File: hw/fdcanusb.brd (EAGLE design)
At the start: 41 x 32 mm, 37 parts, among them J1 MF-CON-MICROUSB-RIGHT, J3 JST-ZH6SMT_VERT, M1 MOUNT, M2 MOUNT, M3 MOUNT, M4 MOUNT, U1 MF-REG-SOT235-3.3V-300mA, U2 USBLC6-2SC6, U3 TCAN334G, U4 TLP3317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

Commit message: Fix resistor footprint
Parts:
- R5: device mfpassives:R0805 -> mfpassives:R0603
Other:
- board text added: "mjbots fdcanusb r2.5 (c) 2021"
- board text removed: "mjbots fdcanusb r2.4 (c) 2021"
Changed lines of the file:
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@@
 <wire x1="41" y1="32" x2="0" y2="32" width="0" layer="20"/>
 <wire x1="0" y1="32" x2="0" y2="0" width="0" layer="20"/>
-<text x="10" y="24.4" size="1" layer="21">mjbots fdcanusb r2.4
+<text x="10" y="24.4" size="1" layer="21">mjbots fdcanusb r2.5
 (c) 2021</text>
 <text x="2.5" y="7.2" size="0.8" layer="21" rot="R180">G</text>
@@
 <attribute name="POPULATE" value="0" x="5" y="8" size="1.778" layer="27" display="off"/>
 </element>
-<element name="R5" library="mfpassives" package="R0805" value="120" x="28.5" y="22.4" smashed="yes" rot="R90">
+<element name="R5" library="mfpassives" package="R0603" value="120" x="28.5" y="22.4" smashed="yes" rot="R90">
 <attribute name="HOUSEPART" value="" x="28.5" y="22.4" size="1.778" layer="27" rot="R90" display="off"/>
 <attribute name="MF" value="YAGEO" x="28.5" y="22.4" size="1.778" layer="27" rot="R90" display="off"/>
@@
 <wire x1="23.7317" y1="25.3067" x2="23.285" y2="24.86" width="0.2159" layer="1"/>
 <wire x1="23.7317" y1="26.1525625" x2="23.7317" y2="25.3067" width="0.2159" layer="1"/>
-<wire x1="28.5" y1="21.45" x2="28.5" y2="20.5683" width="0.2159" layer="1"/>
+<wire x1="28.5" y1="21.65" x2="28.5" y2="20.5683" width="0.2159" layer="1"/>
 </signal>
 <signal name="N$3">
@@
 <contactref element="R5" pad="P$2"/>
 <contactref element="U4" pad="3"/>
-<wire x1="28.5" y1="23.35" x2="29.45" y2="23.35" width="0.254" layer="1"/>
-<wire x1="29.45" y1="23.35" x2="29.8" y2="23" width="0.254" layer="1"/>
+<wire x1="28.5" y1="23.15" x2="29.742678125" y2="23.15" width="0.254" layer="1"/>
+<wire x1="29.767390625" y1="23.032609375" x2="29.742678125" y2="23.15" width="0.254" layer="1"/>
+<wire x1="29.8" y1="23" x2="29.767390625" y2="23.032609375" width="0.254" layer="1"/>
 <via x="29.8" y="23" extent="1-16" drill="0.35"/>
 <wire x1="29.8" y1="23" x2="29.8" y2="19" width="0.254" layer="16"/>

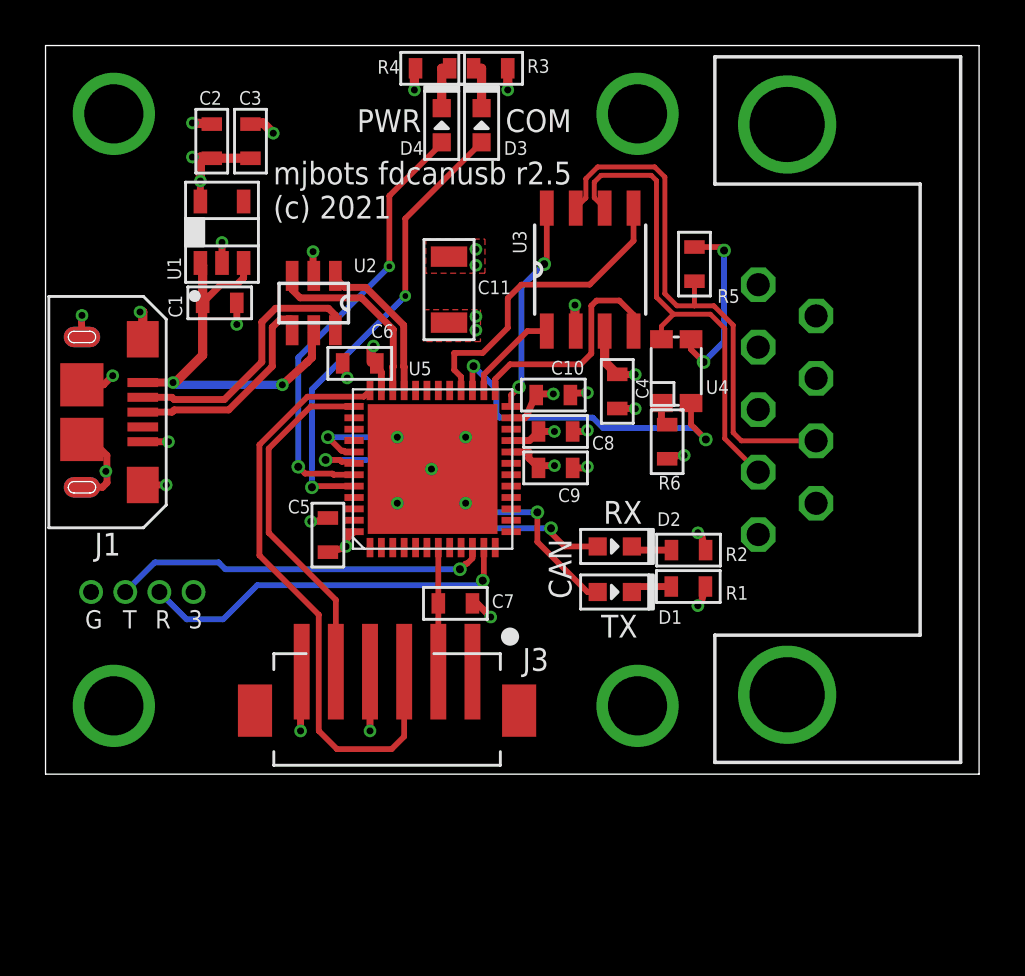
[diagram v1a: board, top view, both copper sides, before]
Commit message: SCHEMATIC ONLY work on more CAN transceiver variants
Update schematic, but not PCB, to accept the TCAN1057AEV in addition
to the 3.3V native variants.
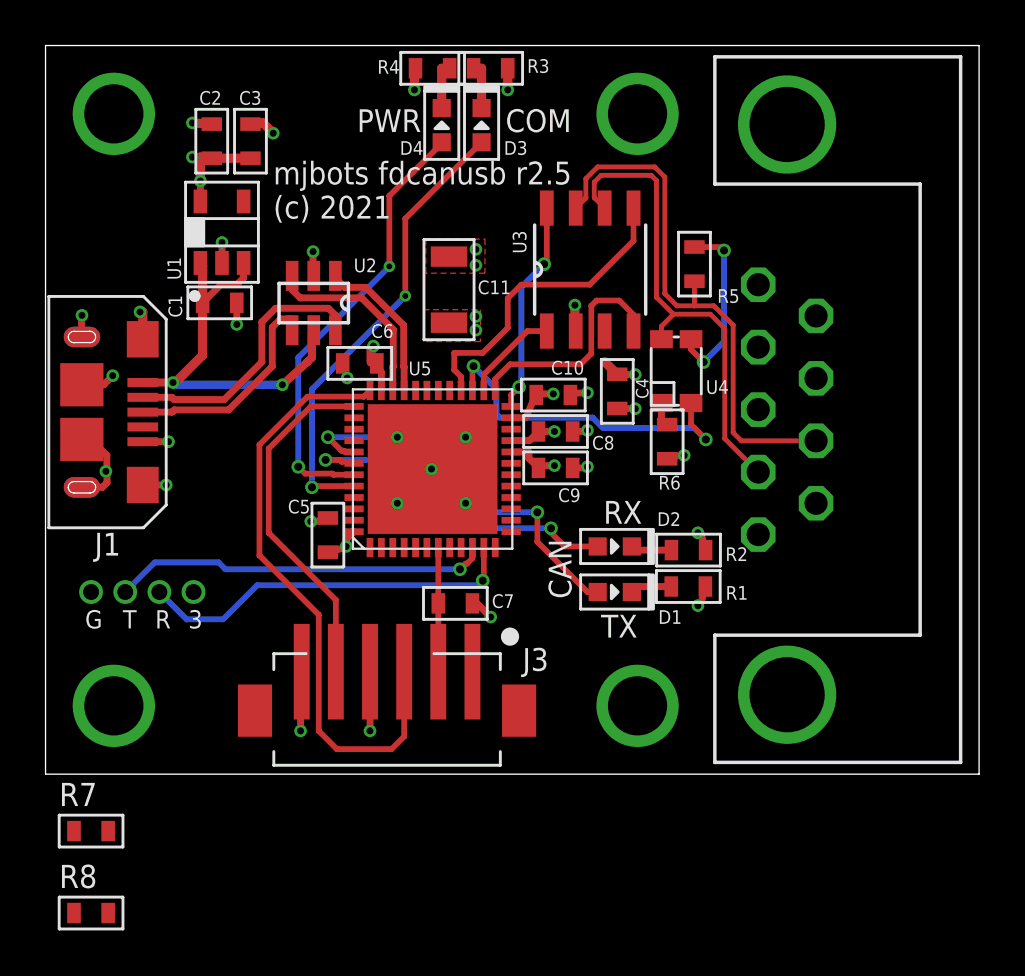
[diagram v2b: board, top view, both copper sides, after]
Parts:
- added R7: DNP, mfpassives:R0603
- added R8: 0, mfpassives:R0603
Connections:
- new net N$1: R7.P$2, R8.P$2, U3.3
- net +3V3: now also R7.P$1; no longer U3.3
- net VBUS: now also R8.P$1
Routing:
- net +3V3: track 22.2 -> 20.9 mm
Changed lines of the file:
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@@
 <param name="tpViaShape" value="round"/>
 <param name="PrefDir.1" value="|"/>
-<param name="PrefDir.2" value="/"/>
+<param name="PrefDir.2" value="0"/>
 <param name="PrefDir.3" value="0"/>
 <param name="PrefDir.4" value="0"/>
@@
 <param name="PrefDir.13" value="0"/>
 <param name="PrefDir.14" value="0"/>
-<param name="PrefDir.15" value="\"/>
+<param name="PrefDir.15" value="0"/>
 <param name="PrefDir.16" value="-"/>
 <param name="cfVia" value="8"/>
@@
 <attribute name="VOLTAGE" value="" x="27.3" y="14.6" size="1.778" layer="27" rot="R90" display="off"/>
 <attribute name="WATTAGE" value="" x="27.3" y="14.6" size="1.778" layer="27" rot="R90" display="off"/>
+</element>
+<element name="R7" library="mfpassives" package="R0603" value="DNP" x="2" y="-2.5" smashed="yes">
+<attribute name="HOUSEPART" value="YES" x="2" y="-2.5" size="1.778" layer="27" display="off"/>
+<attribute name="MPN" value="" x="2" y="-2.5" size="1.778" layer="27" display="off"/>
+<attribute name="NAME" x="0.6" y="-1.4" size="1.016" layer="25" font="vector" ratio="16"/>
+<attribute name="POPULATE" value="0" x="2" y="-2.5" size="1.778" layer="27" display="off"/>
+<attribute name="TOLERANCE" value="" x="2" y="-2.5" size="1.778" layer="27" display="off"/>
+<attribute name="URL" value="" x="2" y="-2.5" size="1.778" layer="27" display="off"/>
+<attribute name="VOLTAGE" value="" x="2" y="-2.5" size="1.778" layer="27" display="off"/>
+<attribute name="WATTAGE" value="" x="2" y="-2.5" size="1.778" layer="27" display="off"/>
+</element>
+<element name="R8" library="mfpassives" package="R0603" value="0" x="2" y="-6.1" smashed="yes">
+<attribute name="HOUSEPART" value="YES" x="2" y="-6.1" size="1.778" layer="27" display="off"/>
+<attribute name="MPN" value="MF-RES-0603-0" x="2" y="-6.1" size="1.778" layer="27" display="off"/>
+<attribute name="NAME" x="0.6" y="-5" size="1.016" layer="25" font="vector" ratio="16"/>
+<attribute name="POPULATE" value="1" x="2" y="-6.1" size="1.778" layer="27" display="off"/>
+<attribute name="TOLERANCE" value="" x="2" y="-6.1" size="1.778" layer="27" display="off"/>
+<attribute name="URL" value="" x="2" y="-6.1" size="1.778" layer="27" display="off"/>
+<attribute name="VOLTAGE" value="" x="2" y="-6.1" size="1.778" layer="27" display="off"/>
+<attribute name="WATTAGE" value="" x="2" y="-6.1" size="1.778" layer="27" display="off"/>
 </element>
 </elements>
@@
 <wire x1="10.4" y1="17.1" x2="5.7" y2="17.1" width="0.3556" layer="16"/>
 <wire x1="5.7" y1="17.1" x2="5.6" y2="17.2" width="0.3556" layer="16"/>
+<contactref element="R8" pad="P$1"/>
+<wire x1="1.25" y1="-6.1" x2="4.27" y2="17.2" width="0" layer="19" extent="1-1"/>
 </signal>
 <signal name="USB_D_N" class="1">
@@
 <contactref element="C3" pad="P$1"/>
 <contactref element="C4" pad="P$1"/>
-<contactref element="U3" pad="3"/>
 <contactref element="C8" pad="P$1"/>
 <contactref element="C9" pad="P$1"/>
@@
 <wire x1="13.2" y1="10" x2="13.2" y2="10.3" width="0.3048" layer="1"/>
 <wire x1="13.2" y1="10.3" x2="13.55" y2="10.65" width="0.3048" layer="1"/>
-<wire x1="24.555" y1="19.46" x2="24.555" y2="18.115" width="0.4064" layer="1"/>
 <wire x1="24.555" y1="18.115" x2="25.11" y2="17.56" width="0.4064" layer="1"/>
 <wire x1="21.65" y1="13.45" x2="21.23" y2="13.87" width="0.3048" layer="1"/>
@@
 <wire x1="21.65" y1="13.45" x2="21.75" y2="13.55" width="0.3048" layer="1"/>
 <wire x1="21.75" y1="13.55" x2="22.35" y2="13.55" width="0.3048" layer="1"/>
+<contactref element="R7" pad="P$1"/>
+<wire x1="25.9" y1="17.55" x2="27.3" y2="13.85" width="0" layer="19" extent="1-1"/>
+<wire x1="22.3" y1="16.7" x2="24.555" y2="18.115" width="0" layer="19" extent="1-1"/>
+<wire x1="20.45" y1="14.65" x2="20.45" y2="15.65" width="0" layer="19" extent="1-1"/>
+<wire x1="20.45" y1="14.15" x2="20.45" y2="14.65" width="0" layer="19" extent="1-1"/>
+<wire x1="18.9" y1="19.5" x2="21.55" y2="16.65" width="0" layer="19" extent="1-1"/>
+<wire x1="18.9" y1="20.1" x2="18.9" y2="19.5" width="0" layer="19" extent="1-1"/>
+<wire x1="17.72" y1="19.83" x2="18.9" y2="19.5" width="0" layer="19" extent="1-1"/>
+<wire x1="14.4" y1="18.8" x2="17.72" y2="19.83" width="0" layer="19" extent="1-1"/>
+<wire x1="13.55" y1="10.65" x2="14.75" y2="16.85" width="0" layer="19" extent="1-1"/>
+<wire x1="11.25" y1="4.5" x2="12.4" y2="9.75" width="0" layer="19" extent="1-1"/>
+<wire x1="6.5" y1="8" x2="11.25" y2="4.5" width="0" layer="19" extent="1-1"/>
+<wire x1="9" y1="27.05" x2="14.4" y2="18.8" width="0" layer="19" extent="1-1"/>
+<wire x1="1.25" y1="-2.5" x2="11.2" y2="1.9" width="0" layer="19" extent="1-1"/>
 </signal>
 <signal name="NRST">
@@
 <wire x1="27.3" y1="15.35" x2="27.05" y2="15.4" width="0.3048" layer="1"/>
 </signal>
+<signal name="N$1">
+<contactref element="U3" pad="3"/>
+<contactref element="R7" pad="P$2"/>
+<contactref element="R8" pad="P$2"/>
+<wire x1="2.75" y1="-2.5" x2="24.555" y2="19.46" width="0" layer="19" extent="1-1"/>
+<wire x1="2.75" y1="-6.1" x2="2.75" y2="-2.5" width="0" layer="19" extent="1-1"/>
+</signal>
 </signals>

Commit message: Nominally complete fdcanusb w/ support for all known SOIC8/SOT8 CAN
* This will work with all the 3.3V and 5V 8 pin parts I know of with
  no more than different resistor populations.
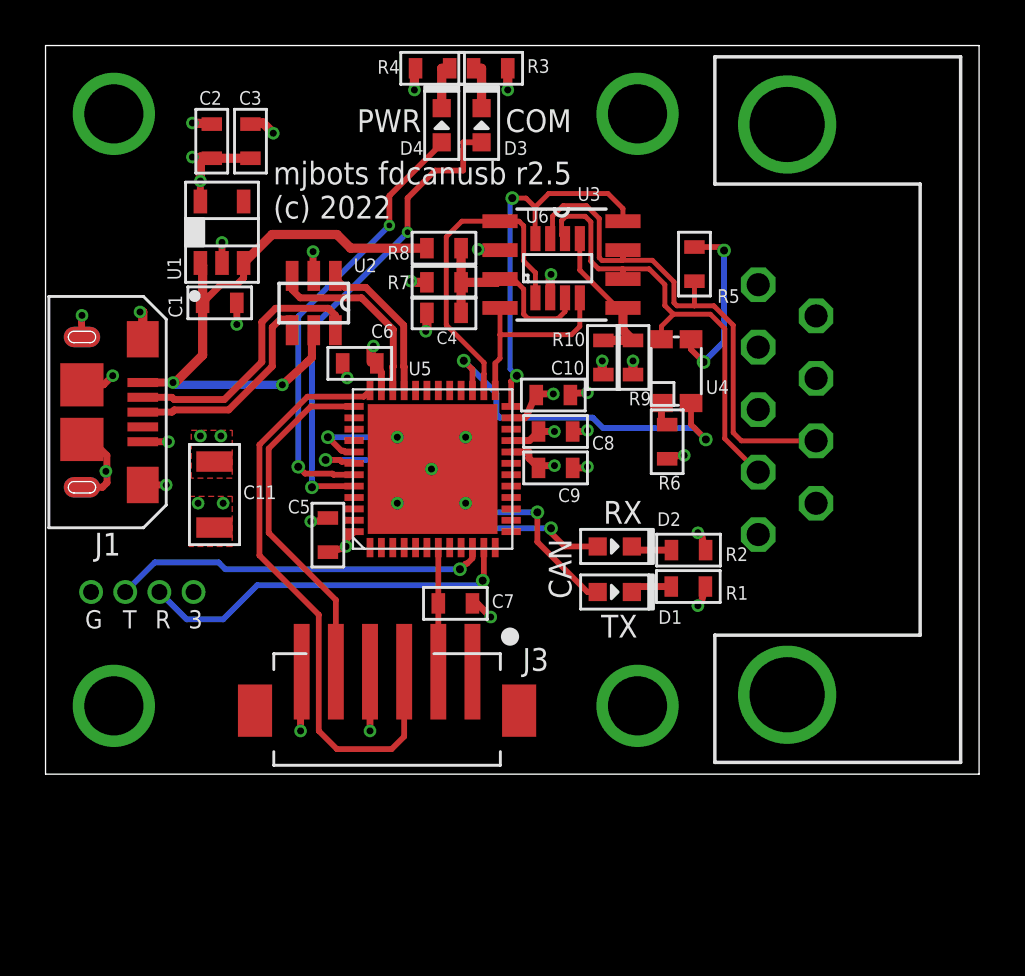
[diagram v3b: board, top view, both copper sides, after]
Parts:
- added R10: 0, mfpassives:R0603
- added R9: DNP, mfpassives:R0603
- added U6: TCAN334GSOT23-8-NOPASTE, controller:SOT23-8-NOPASTE
- U3: value TCAN334G -> TCAN1057AEV
- moved R8 33.1 mm to (17.5, 23.1)
- moved R7 28.7 mm to (17.5, 21.6)
- moved C11 13.7 mm to (7.42, 12.3)
- moved C4 8.36 mm to (17.5, 20.3), turned to 180 degrees
- moved U3 1.28 mm to (22.7, 22.4), turned to 0 degrees
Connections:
- removed net CAN_SHDN: U3.5, U5.28
- new net CAN_SHDN_VIO: R10.P$1, R9.P$2, U3.5, U6.5
- net +3V3: now also R10.P$2; no longer C4.P$1
- net CAN_N: now also U6.6
- net CAN_P: now also U6.7
- net CAN_RX: now also U6.4
- net CAN_STB: now also U6.8
- net CAN_TX: now also U6.1
- net GND: now also R9.P$1, U6.2
- net N$1: now also C4.P$1, U6.3
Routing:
- net CAN_SHDN: track 13.9 -> 0.00 mm
- net CAN_TX: track 4.26 -> 14.6 mm
- net N$1: track 0.00 -> 9.57 mm
- net VBUS: track 18.0 -> 26.8 mm
- net CAN_STB: track 9.36 -> 16.9 mm
- net CAN_SHDN_VIO: track 0.00 -> 6.87 mm
- net CAN_RX: track 10.2 -> 8.62 mm
- net GND: track 27.8 -> 29.3 mm, vias 31 -> 33
- net LED_COM: track 20.1 -> 21.3 mm
- net CAN_TERM: track 15.1 -> 15.9 mm
- net +3V3: track 20.9 -> 20.7 mm, vias 12 -> 13
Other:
- board text added: "mjbots fdcanusb r2.5 (c) 2022"
- board text removed: "mjbots fdcanusb r2.5 (c) 2021"
